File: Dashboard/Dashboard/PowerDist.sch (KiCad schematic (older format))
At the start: 15 parts, among them J3 CarPowerConnector, U2 RI3-1205S, U3 NCP1117-3.3_SOT223

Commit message: Make major changes to Dashboard and file structure.
Problem
=======
* The dashboard needs to be redesigned. These are continuing changes
to Dashboard 2.0.
* There are way too many files cluttering the Dashboard folder.
* We need to include LED indicators for the driver that make sense.

Solution
========
* I made major changes to the dashboard. These include the following:
  * Add an external LED board to mount on the steering wheel.
  * Add hardware timer circuitry for lights, so that the software does
    not have to concern itself with the flashers.
  * Generally cleaned up the dashboard's schematics
* There have also been changes made to the file system. All extra files
  that were not necessary have been removed. In the future, reference
  materials should be kept outside of version control.

Notes
=====
The dashboard still is not complete. We still need to address the following:
1. Pin assignments right now are mostly arbitrary. They are still subject to change.
2. The design needs to be verified.
3. We need to settle on the interface. Things like the ignition dial are still
   possible to change if we desire.
4. We need to add another potentiometer for the accelerator. This is missing because
   it was previously handled by the motor interface board.
5. Probably some other things that I'm forgetting.
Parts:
- removed J3: CarPowerConnector, UTSVT_Connectors:Molex_MicroFit3.0_1x2xP3.00mm_PolarizingPeg_Vertical, symbol utsvt-connectors:CarPowerConnector
- removed L4: SRF0905-100Y, UTSVT_BPS:SRF0905A, symbol utsvt-bps:SRF0905-100Y
- removed U2: RI3-1205S, UTSVT_ICs:RI3_DC_Converter, symbol utsvt-power-regulators:RI3-1205S
- added J301: CarPowerConnector, utsvt_conn:Molex_MicroFit3.0_1x2xP3.00mm_PolarizingPeg_Vertical, symbol Conn:CarPowerConnector
- added L301: SRF0905-100Y, utsvt_bps:SRF0905A, symbol BPS:SRF0905-100Y
- added U301: RI3-1205S, utsvt_ics:RI3_DC_Converter, symbol Power:RI3-1205S
- C301: renamed from C14; Mouser Part Number (none) -> 80-C0805C475K3RAUTO
- C302: renamed from C15; value 0.1uF -> 10uF; Mouser Part Number (none) -> 80-C0805C106K8RAUTO
- C303: renamed from C16; Mouser Part Number (none) -> 80-C0805C471J5HACTU
- C304: renamed from C17; Mouser Part Number (none) -> 80-C0805C106K8RAUTO
- D301: renamed from D1; Mouser Part Number (none) -> 604-APTD2012LCGCK
- R301: renamed from R1; Mouser Part Number (none) -> 71-CRCW08051K50FKEAC
- U302: renamed from U3; Mouser Part Number (none) -> 863-NCP1117ST33T3G
- renumbered TP1 to TP301, TP2 to TP302, TP3 to TP303, TP4 to TP304, TP5 to TP305
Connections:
- wire segments 60 -> 64
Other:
- moved on the sheet: C301, D301, R301, TP301, TP302

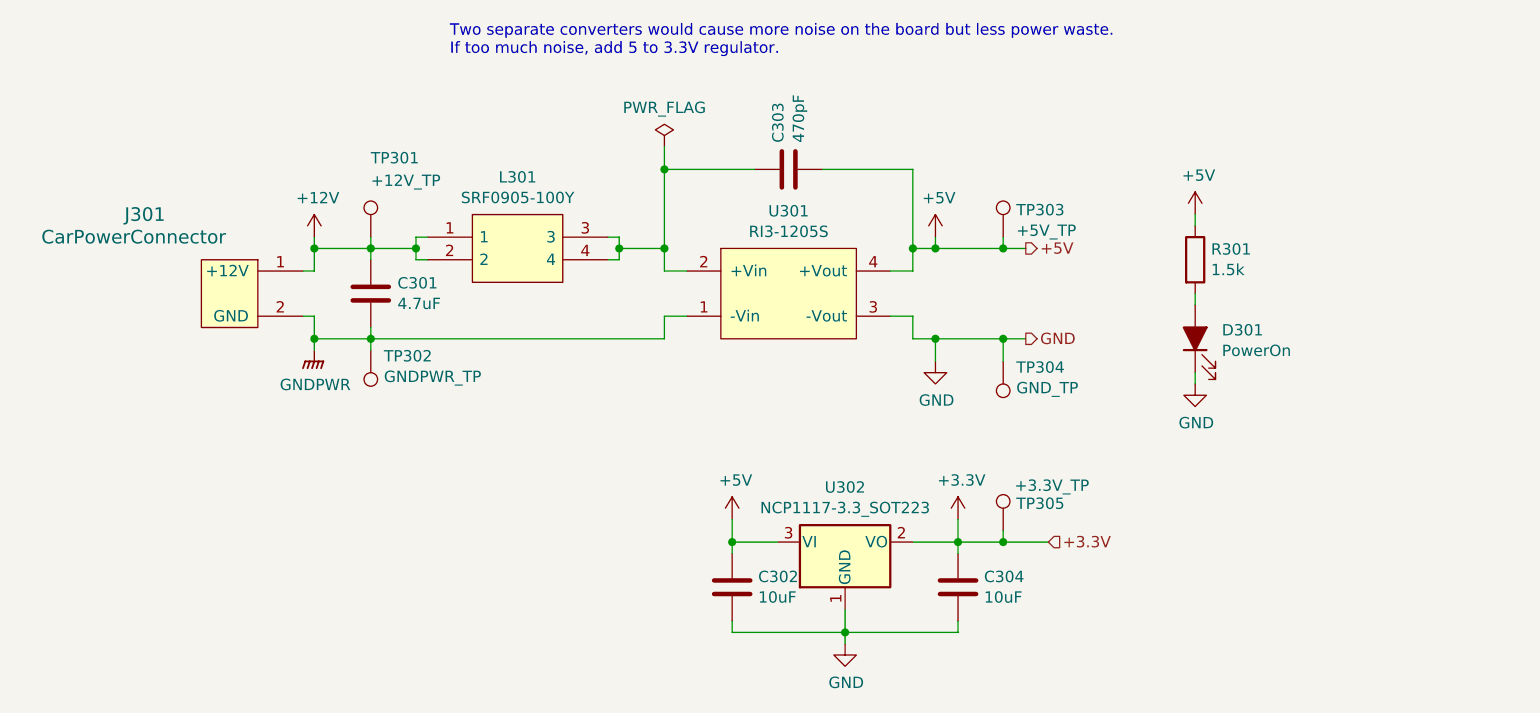
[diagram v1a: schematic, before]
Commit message: Add redundant potentiometers and relabel components.
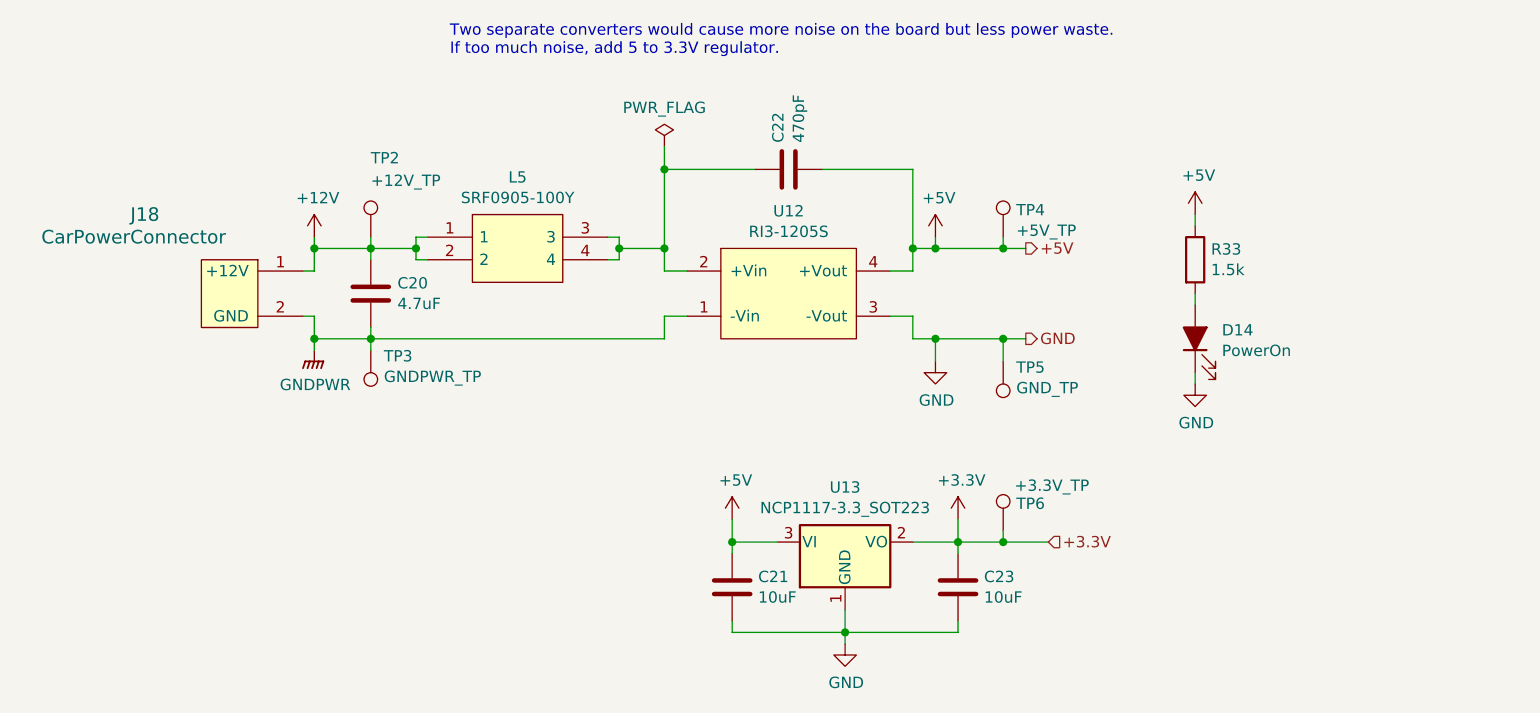
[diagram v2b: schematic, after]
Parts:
- renumbered C301 to C20, C302 to C21, C303 to C22, C304 to C23, D301 to D14, J301 to J18, L301 to L5, R301 to R33, TP301 to TP2, TP302 to TP3, TP303 to TP4, TP304 to TP5, TP305 to TP6, U301 to U12, U302 to U13
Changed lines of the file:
@@
 	2450 3500 2450 3600
 $Comp
-L power:+12V #PWR0301
+L power:+12V #PWR078
 U 1 1 5C35F2D2
 P 2450 3150
-F 0 "#PWR0301" H 2450 3000 50  0001 C CNN
+F 0 "#PWR078" H 2450 3000 50  0001 C CNN
 F 1 "+12V" H 2465 3323 50  0000 C CNN
 F 2 "" H 2450 3150 50  0001 C CNN
@@
 	2450 3600 2450 3650
 $Comp
-L Device:C C301
+L Device:C C20
 U 1 1 5C35F7E4
 P 2700 3400
-F 0 "C301" H 2818 3446 50  0000 L CNN
+F 0 "C20" H 2818 3446 50  0000 L CNN
 F 1 "4.7uF" H 2818 3355 50  0000 L CNN
 F 2 "Capacitor_SMD:C_0805_2012Metric" H 2738 3250 50  0001 C CNN
@@
 Connection ~ 5200 3600
 $Comp
-L Device:C C303
+L Device:C C22
 U 1 1 5C3626E7
 P 4550 2850
-F 0 "C303" H 4668 2896 50  0000 L CNN
+F 0 "C22" H 4668 2896 50  0000 L CNN
 F 1 "470pF" H 4668 2805 50  0000 L CNN
 F 2 "Capacitor_SMD:C_2220_5650Metric" H 4588 2700 50  0001 C CNN
@@
 +5V
 $Comp
-L power:+5V #PWR0305
+L power:+5V #PWR082
 U 1 1 5C376123
 P 5200 3150
-F 0 "#PWR0305" H 5200 3000 50  0001 C CNN
+F 0 "#PWR082" H 5200 3000 50  0001 C CNN
 F 1 "+5V" H 5215 3323 50  0000 C CNN
 F 2 "" H 5200 3150 50  0001 C CNN
@@
 $EndComp
 $Comp
-L Connector:TestPoint TP301
+L Connector:TestPoint TP2
 U 1 1 5C37D606
 P 2700 3150
-F 0 "TP301" H 2700 3500 50  0000 L CNN
+F 0 "TP2" H 2700 3500 50  0000 L CNN
 F 1 "+12V_TP" H 2700 3400 50  0000 L CNN
 F 2 "TestPoint:TestPoint_Keystone_5005-5009_Compact" H 2900 3150 50  0001 C CNN
@@
 	2700 3150 2700 3200
 $Comp
-L Connector:TestPoint TP303
+L Connector:TestPoint TP4
 U 1 1 5C37E6A3
 P 5500 3150
-F 0 "TP303" H 5558 3270 50  0000 L CNN
+F 0 "TP4" H 5558 3270 50  0000 L CNN
 F 1 "+5V_TP" H 5558 3179 50  0000 L CNN
 F 2 "TestPoint:TestPoint_Keystone_5005-5009_Compact" H 5700 3150 50  0001 C CNN
@@
 	5500 3150 5500 3200
 $Comp
-L Connector:TestPoint TP304
+L Connector:TestPoint TP5
 U 1 1 5C37F6B1
 P 5500 3700
-F 0 "TP304" H 5442 3727 50  0000 R CNN
+F 0 "TP5" H 5442 3727 50  0000 R CNN
 F 1 "GND_TP" H 5442 3818 50  0000 R CNN
 F 2 "TestPoint:TestPoint_Keystone_5005-5009_Compact" H 5700 3700 50  0001 C CNN
@@
 	5500 3700 5500 3600
 $Comp
-L power:GND #PWR0309
+L power:GND #PWR086
 U 1 1 5C58D746
 P 6350 3800
-F 0 "#PWR0309" H 6350 3550 50  0001 C CNN
+F 0 "#PWR086" H 6350 3550 50  0001 C CNN
 F 1 "GND" H 6355 3627 50  0000 C CNN
 F 2 "" H 6350 3800 50  0001 C CNN
@@
 $EndComp
 $Comp
-L Device:LED_ALT D301
+L Device:LED_ALT D14
 U 1 1 5C58D83E
 P 6350 3600
-F 0 "D301" V 6388 3482 50  0000 R CNN
+F 0 "D14" V 6388 3482 50  0000 R CNN
 F 1 "PowerOn" V 6297 3482 50  0000 R CNN
 F 2 "LED_SMD:LED_0805_2012Metric" H 6350 3600 50  0001 C CNN
@@
 $EndComp
 $Comp
-L Device:R R301
+L Device:R R33
 U 1 1 5C58D993
 P 6350 3250
-F 0 "R301" H 6420 3296 50  0000 L CNN
+F 0 "R33" H 6420 3296 50  0000 L CNN
 F 1 "1.5k" H 6420 3205 50  0000 L CNN
 F 2 "Resistor_SMD:R_0805_2012Metric" V 6280 3250 50  0001 C CNN
@@
 	6350 3450 6350 3400
 $Comp
-L power:+5V #PWR0308
+L power:+5V #PWR085
 U 1 1 5C58FEF6
 P 6350 3050
-F 0 "#PWR0308" H 6350 2900 50  0001 C CNN
+F 0 "#PWR085" H 6350 2900 50  0001 C CNN
 F 1 "+5V" H 6365 3223 50  0000 C CNN
 F 2 "" H 6350 3050 50  0001 C CNN
@@
 	6350 3050 6350 3100
 $Comp
-L power:GND #PWR0306
+L power:GND #PWR083
 U 1 1 5C3F3B1F
 P 5200 3700
-F 0 "#PWR0306" H 5200 3450 50  0001 C CNN
+F 0 "#PWR083" H 5200 3450 50  0001 C CNN
 F 1 "GND" H 5205 3527 50  0000 C CNN
 F 2 "" H 5200 3700 50  0001 C CNN
@@
 $EndComp
 $Comp
-L power:GNDPWR #PWR0302
+L power:GNDPWR #PWR079
 U 1 1 5C3F7204
 P 2450 3650
-F 0 "#PWR0302" H 2450 3450 50  0001 C CNN
+F 0 "#PWR079" H 2450 3450 50  0001 C CNN
 F 1 "GNDPWR" H 2454 3496 50  0000 C CNN
 F 2 "" H 2450 3600 50  0001 C CNN
@@
 $EndComp
 $Comp
-L power:+5V #PWR0303
+L power:+5V #PWR080
 U 1 1 5C702374
 P 4300 4400
-F 0 "#PWR0303" H 4300 4250 50  0001 C CNN
+F 0 "#PWR080" H 4300 4250 50  0001 C CNN
 F 1 "+5V" H 4315 4573 50  0000 C CNN
 F 2 "" H 4300 4400 50  0001 C CNN
@@
 $EndComp
 $Comp
-L Regulator_Linear:LD1117S33TR_SOT223 U302
+L Regulator_Linear:LD1117S33TR_SOT223 U13
 U 1 1 5C70247C
 P 4800 4500
-F 0 "U302" H 4800 4742 50  0000 C CNN
+F 0 "U13" H 4800 4742 50  0000 C CNN
 F 1 "NCP1117-3.3_SOT223" H 4800 4651 50  0000 C CNN
 F 2 "Package_TO_SOT_SMD:SOT-223-3_TabPin2" H 4800 4700 50  0001 C CNN
@@
 $EndComp
 $Comp
-L Device:C C302
+L Device:C C21
 U 1 1 5C702937
 P 4300 4700
-F 0 "C302" H 4415 4746 50  0000 L CNN
+F 0 "C21" H 4415 4746 50  0000 L CNN
 F 1 "10uF" H 4415 4655 50  0000 L CNN
 F 2 "Capacitor_SMD:C_0805_2012Metric" H 4338 4550 50  0001 C CNN
@@
 $EndComp
 $Comp
-L Device:C C304
+L Device:C C23
 U 1 1 5C7029C7
 P 5300 4700
-F 0 "C304" H 5415 4746 50  0000 L CNN
+F 0 "C23" H 5415 4746 50  0000 L CNN
 F 1 "10uF" H 5415 4655 50  0000 L CNN
 F 2 "Capacitor_SMD:C_0805_2012Metric" H 5338 4550 50  0001 C CNN
@@
 	5300 4500 5300 4550
 $Comp
-L power:GND #PWR0304
+L power:GND #PWR081
 U 1 1 5C703BF4
 P 4800 4950
-F 0 "#PWR0304" H 4800 4700 50  0001 C CNN
+F 0 "#PWR081" H 4800 4700 50  0001 C CNN
 F 1 "GND" H 4805 4777 50  0000 C CNN
 F 2 "" H 4800 4950 50  0001 C CNN
@@
 Connection ~ 4300 4500
 $Comp
-L power:+3.3V #PWR0307
+L power:+3.3V #PWR084
 U 1 1 5C7065C8
 P 5300 4400
-F 0 "#PWR0307" H 5300 4250 50  0001 C CNN
+F 0 "#PWR084" H 5300 4250 50  0001 C CNN
 F 1 "+3.3V" H 5315 4573 50  0000 C CNN
 F 2 "" H 5300 4400 50  0001 C CNN
@@
 	5700 4500 5500 4500
 $Comp
-L Connector:TestPoint TP305
+L Connector:TestPoint TP6
 U 1 1 5C708412
 P 5500 4450
-F 0 "TP305" H 5558 4570 50  0000 L CNN
+F 0 "TP6" H 5558 4570 50  0000 L CNN
 F 1 "+3.3V_TP" H 5550 4650 50  0000 L CNN
 F 2 "TestPoint:TestPoint_Keystone_5005-5009_Compact" H 5700 4450 50  0001 C CNN
@@
 Connection ~ 5100 3200
 $Comp
-L Connector:TestPoint TP302
+L Connector:TestPoint TP3
 U 1 1 5C82CEA3
 P 2700 3650
-F 0 "TP302" H 2642 3677 50  0000 R CNN
+F 0 "TP3" H 2642 3677 50  0000 R CNN
 F 1 "GNDPWR_TP" H 2642 3768 50  0000 R CNN
 F 2 "TestPoint:TestPoint_Keystone_5005-5009_Compact" H 2900 3650 50  0001 C CNN
@@
 	2900 3200 2900 3150
 $Comp
-L power:PWR_FLAG #FLG0301
+L power:PWR_FLAG #FLG01
 U 1 1 5D8F68D6
 P 4000 2750
-F 0 "#FLG0301" H 4000 2825 50  0001 C CNN
+F 0 "#FLG01" H 4000 2825 50  0001 C CNN
 F 1 "PWR_FLAG" H 4000 2923 50  0000 C CNN
 F 2 "" H 4000 2750 50  0001 C CNN
@@
 Connection ~ 4000 2850
 $Comp
-L Conn:CarPowerConnector J301
+L Conn:CarPowerConnector J18
 U 1 1 5F1C4AA5
 P 2100 3400
-F 0 "J301" H 1700 3750 60  0000 C CNN
+F 0 "J18" H 1700 3750 60  0000 C CNN
 F 1 "CarPowerConnector" H 1650 3650 60  0000 C CNN
 F 2 "utsvt_conn:Molex_MicroFit3.0_1x2xP3.00mm_PolarizingPeg_Vertical" H 2100 3400 60  0001 C CNN
@@
 $EndComp
 $Comp
-L Power:RI3-1205S U301
+L Power:RI3-1205S U12
 U 1 1 5F1C9507
 P 4550 3200
-F 0 "U301" H 4550 3365 50  0000 C CNN
+F 0 "U12" H 4550 3365 50  0000 C CNN
 F 1 "RI3-1205S" H 4550 3274 50  0000 C CNN
 F 2 "utsvt_ics:RI3_DC_Converter" H 4550 3200 50  0001 C CNN
@@
 $EndComp
 $Comp
-L BPS:SRF0905-100Y L301
+L BPS:SRF0905-100Y L5
 U 1 1 5F1CA5EE
 P 2950 3150
-F 0 "L301" H 3350 3415 50  0000 C CNN
+F 0 "L5" H 3350 3415 50  0000 C CNN
 F 1 "SRF0905-100Y" H 3350 3324 50  0000 C CNN
 F 2 "utsvt_bps:SRF0905A" H 3600 3250 50  0001 L CNN
